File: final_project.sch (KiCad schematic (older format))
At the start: 0 parts

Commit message: Merged 8254
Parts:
- added C1: 100uF, symbol pspice:C
- added J1: Conn_01x02_Female, symbol Connector:Conn_01x02_Female
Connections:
- new net +5V: C1.1, J1.1 (Pin_1)
- new net GND: C1.2, J1.2 (Pin_2)

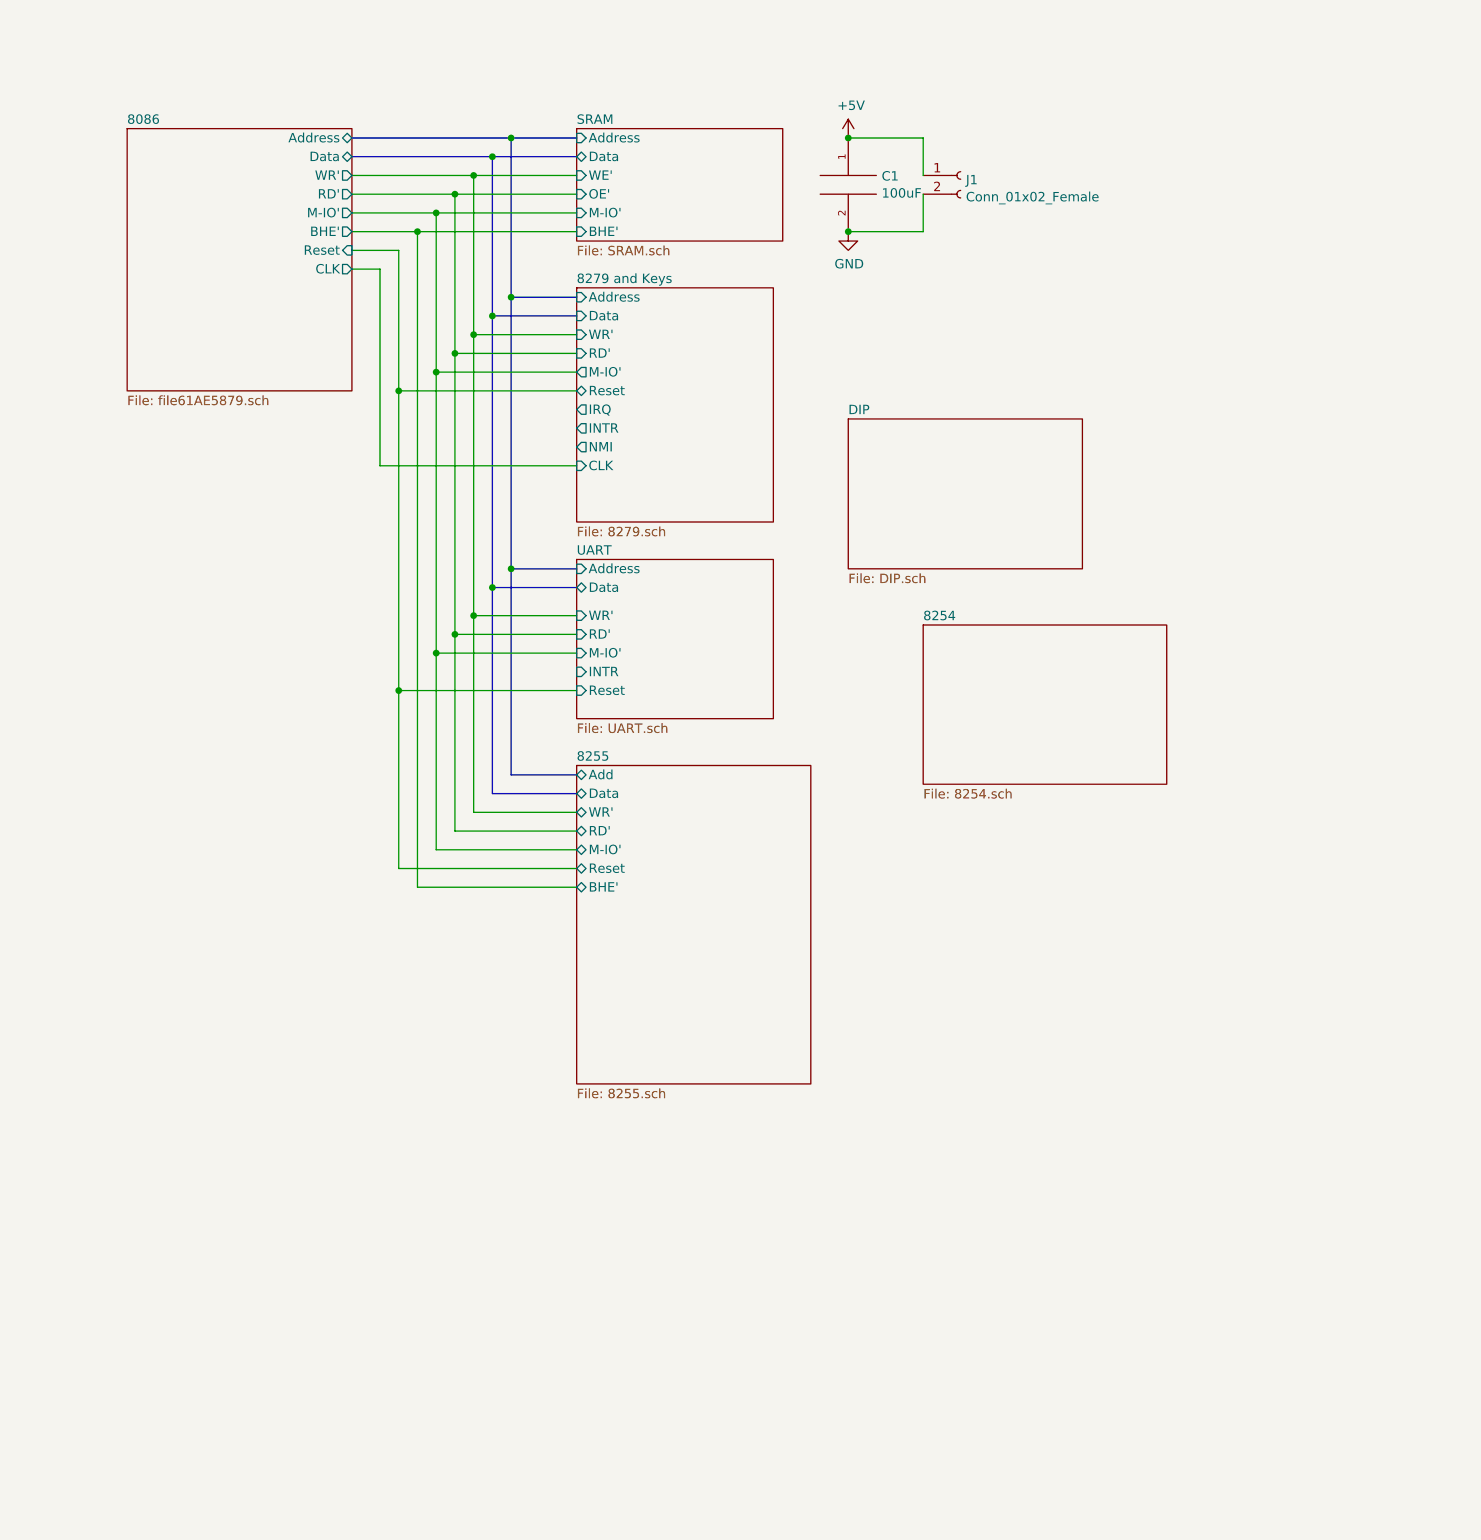
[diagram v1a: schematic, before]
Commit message: Integrated LCD.  Fixed issues with busses
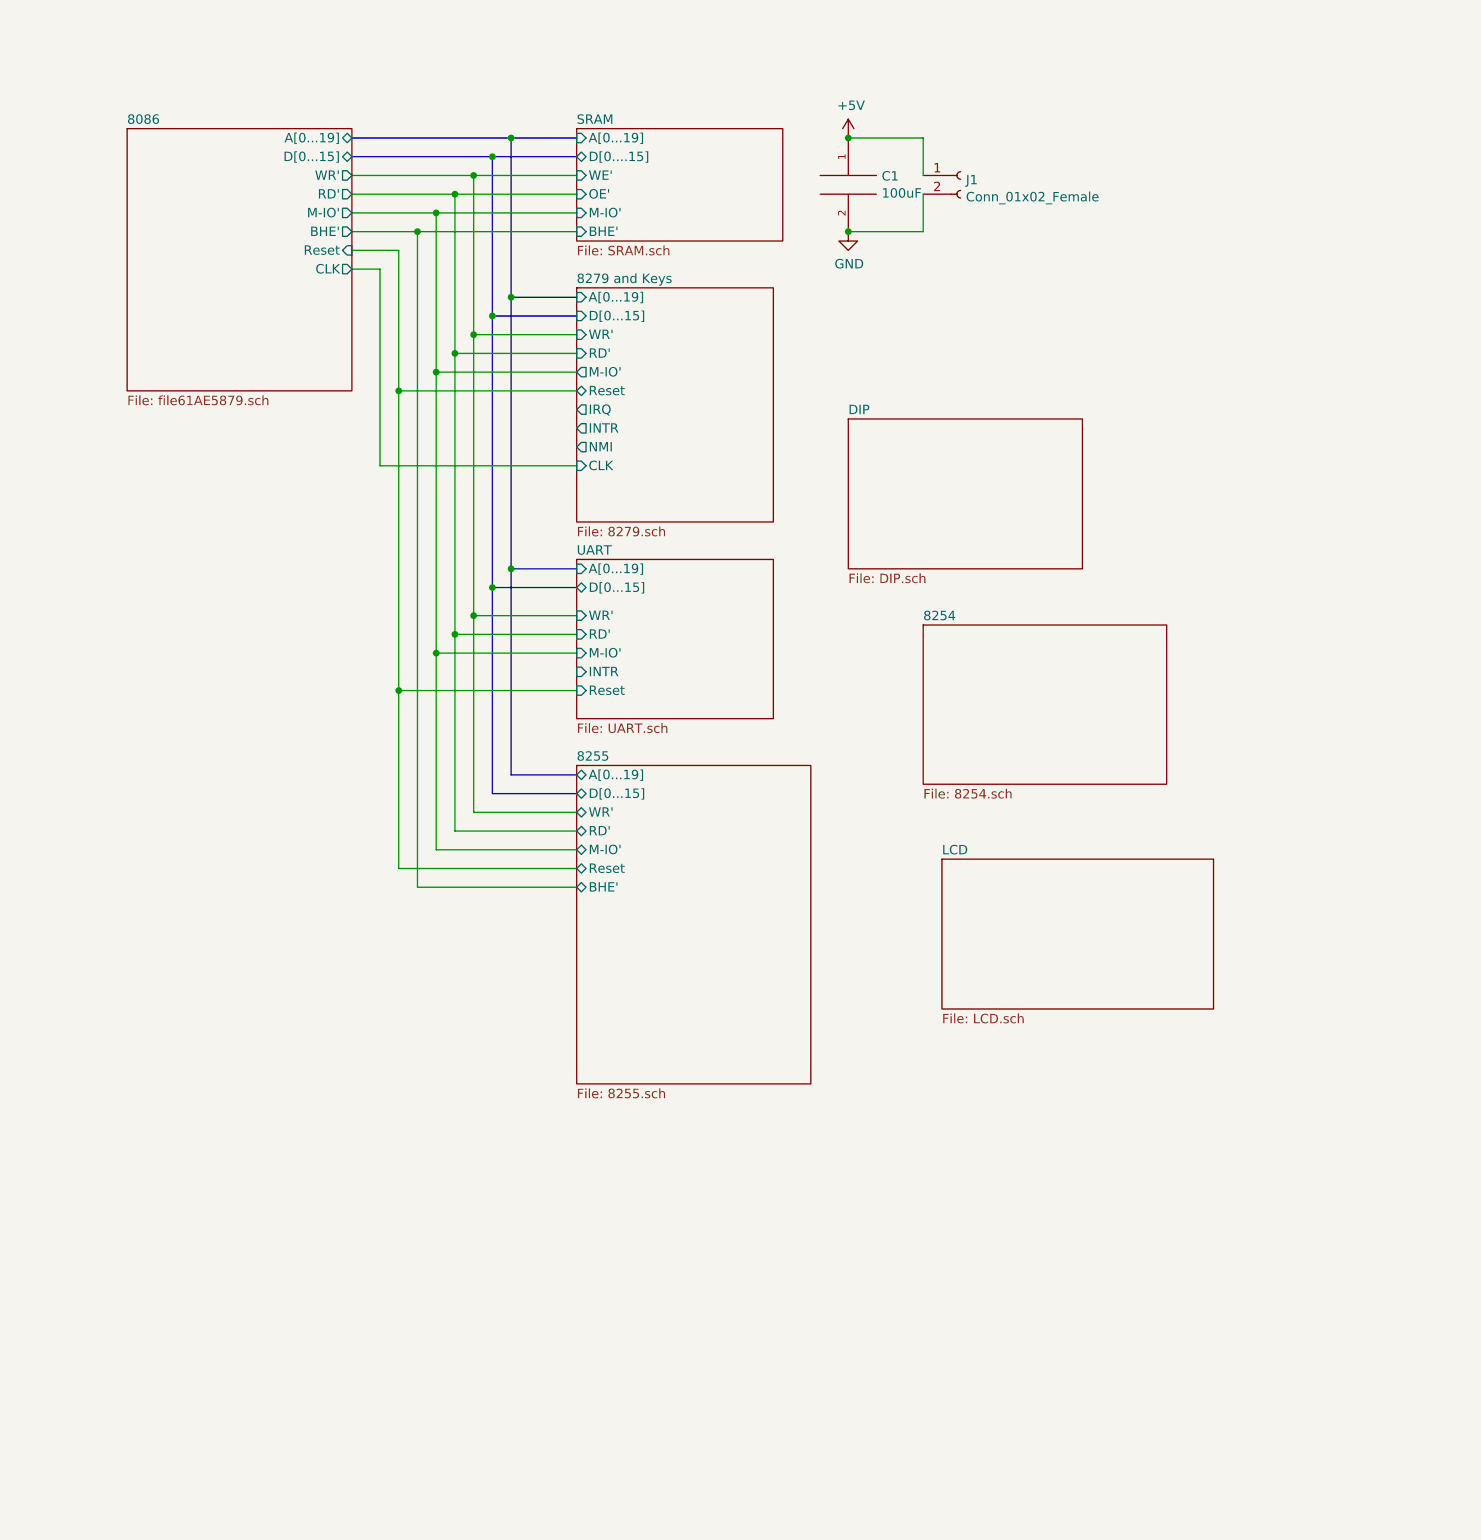
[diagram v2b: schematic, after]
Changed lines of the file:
@@
 $Descr A4 11693 8268
 encoding utf-8
-Sheet 1 8
+Sheet 1 9
 Title ""
 Date ""
@@
 F0 "8086" 50
 F1 "file61AE5879.sch" 50
-F2 "Data" B R 2400 1300 50
-F3 "Address" B R 2400 1200 50
+F2 "D[0...15]" B R 2400 1300 50
+F3 "A[0...19]" B R 2400 1200 50
 F4 "M-IO'" O R 2400 1600 50
 F5 "WR'" O R 2400 1400 50
@@
 F0 "8255" 50
 F1 "8255.sch" 50
-F2 "Data" B L 3600 4700 50
-F3 "Add" B L 3600 4600 50
+F2 "D[0...15]" B L 3600 4700 50
+F3 "A[0...19]" B L 3600 4600 50
 F4 "WR'" B L 3600 4800 50
 F5 "RD'" B L 3600 4900 50
@@
 F0 "8279 and Keys" 50
 F1 "8279.sch" 50
-F2 "Address" I L 3600 2050 50
-F3 "Data" I L 3600 2150 50
+F2 "A[0...19]" I L 3600 2050 50
+F3 "D[0...15]" I L 3600 2150 50
 F4 "WR'" I L 3600 2250 50
 F5 "RD'" I L 3600 2350 50
@@
 F0 "UART" 50
 F1 "UART.sch" 50
-F2 "Data" B L 3600 3600 50
-F3 "Address" I L 3600 3500 50
+F2 "D[0...15]" B L 3600 3600 50
+F3 "A[0...19]" I L 3600 3500 50
 F4 "WR'" I L 3600 3750 50
 F5 "RD'" I L 3600 3850 50
@@
 F2 "BHE'" I L 3600 1700 50
 F3 "WE'" I L 3600 1400 50
-F4 "Address" I L 3600 1200 50
+F4 "A[0...19]" I L 3600 1200 50
 F5 "M-IO'" I L 3600 1600 50
-F6 "Data" B L 3600 1300 50
+F6 "D[0....15]" B L 3600 1300 50
 F7 "OE'" I L 3600 1500 50
 $EndSheet
@@
 $EndComp
 $Comp
-L power:GND #PWR0101
+L power:GND #PWR02
 U 1 1 625BB158
 P 5050 1700
-F 0 "#PWR0101" H 5050 1450 50  0001 C CNN
+F 0 "#PWR02" H 5050 1450 50  0001 C CNN
 F 1 "GND" H 5055 1527 50  0000 C CNN
 F 2 "" H 5050 1700 50  0001 C CNN
@@
 $EndComp
 $Comp
-L power:+5V #PWR0102
+L power:+5V #PWR01
 U 1 1 625BB5A4
 P 5050 1200
-F 0 "#PWR0102" H 5050 1050 50  0001 C CNN
+F 0 "#PWR01" H 5050 1050 50  0001 C CNN
 F 1 "+5V" H 5065 1373 50  0000 C CNN
 F 2 "" H 5050 1200 50  0001 C CNN
@@
 F1 "8254.sch" 50
 $EndSheet
+$Sheet
+S 5550 5050 1450 800
+U 61E46856
+F0 "LCD" 50
+F1 "LCD.sch" 50
+$EndSheet
 $EndSCHEMATC

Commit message: All schematics present
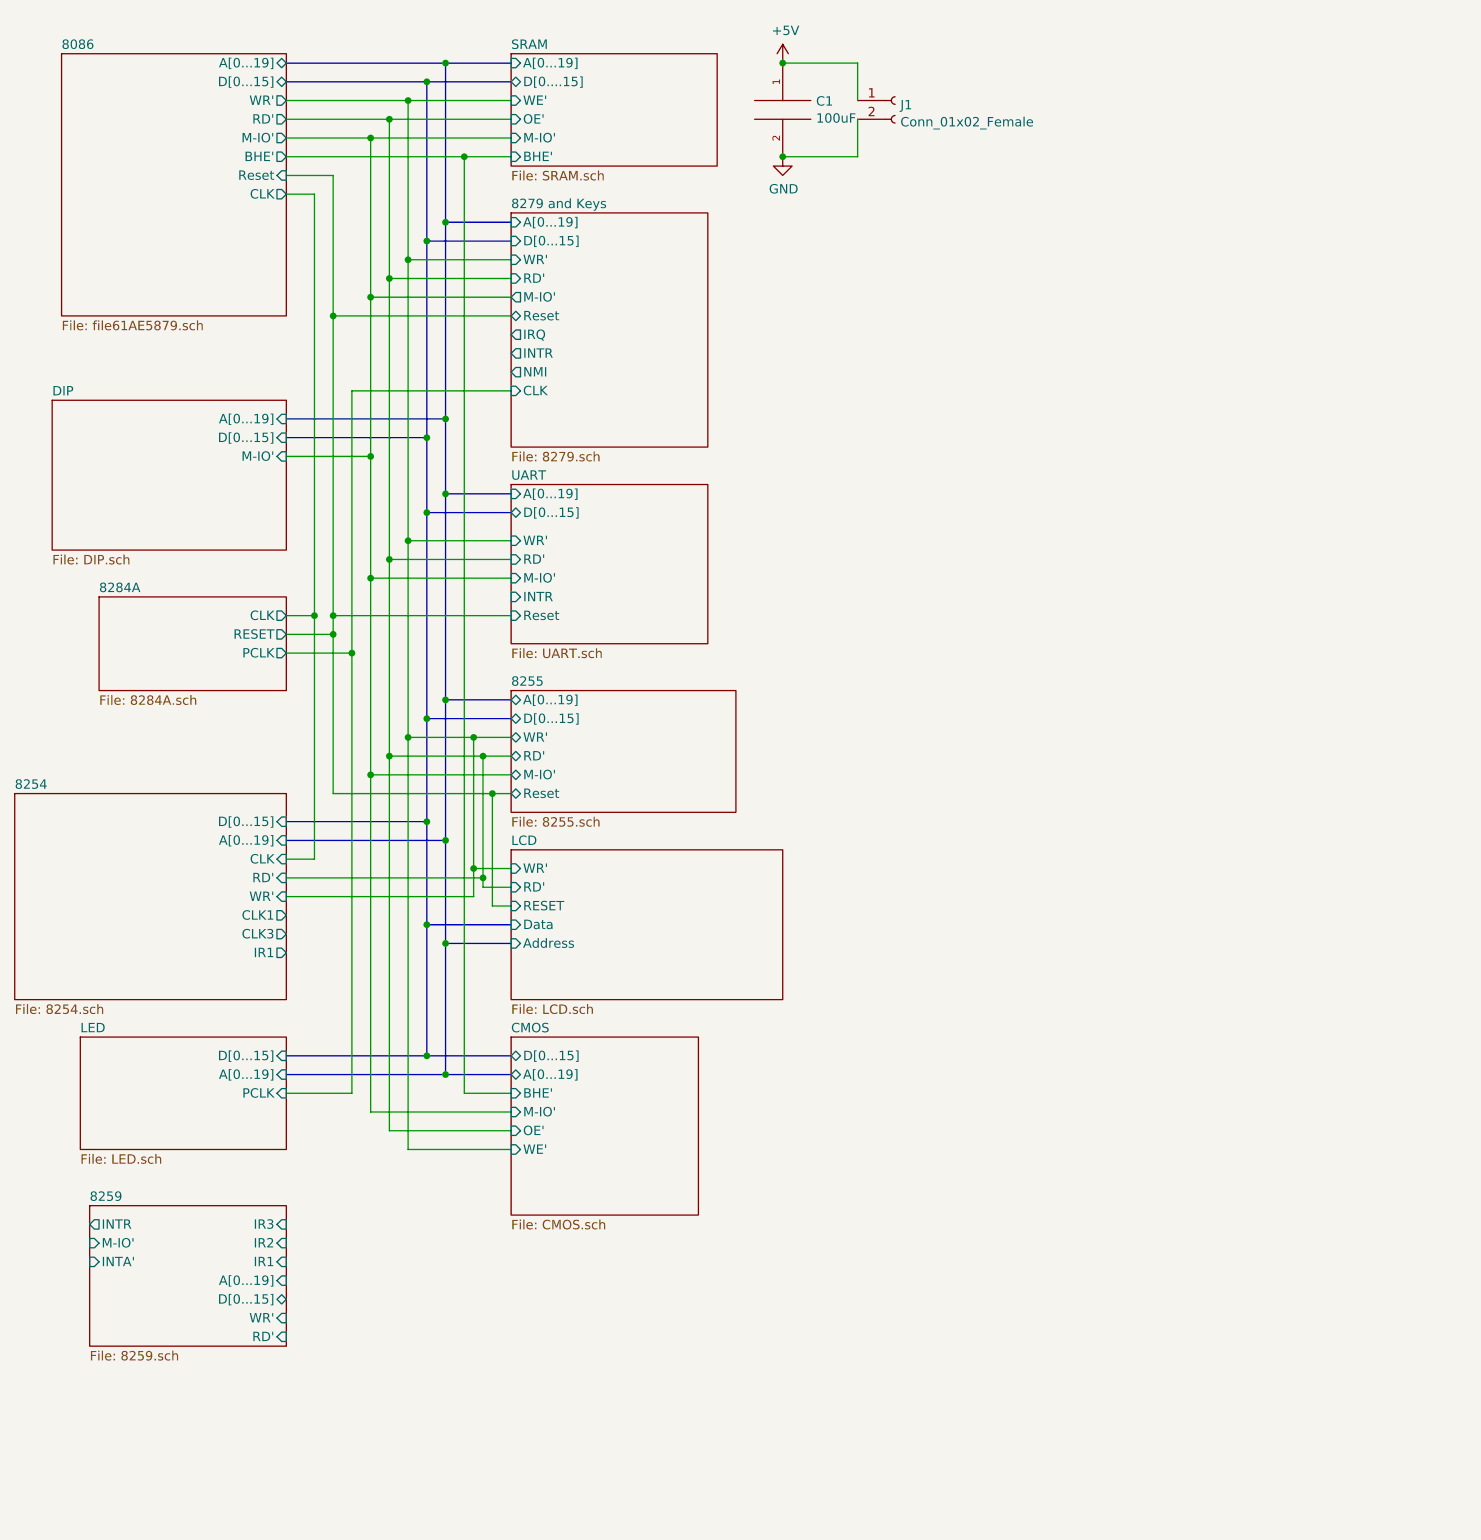
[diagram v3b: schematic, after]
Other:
- moved on the sheet: C1, J1

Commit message: Wired Root
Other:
- moved on the sheet: C1, J1

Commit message: Started PCB
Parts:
- added R1: R, Resistor_SMD:R_0201_0603Metric, symbol Device:R
- C1: footprint (none) -> Capacitor_SMD:CP_Elec_3x5.3
- J1: footprint (none) -> Connector:Banana_Jack_1Pin
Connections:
- net +5V: now also R1.1
- new net +3V3: R1.2
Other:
- moved on the sheet: C1, J1
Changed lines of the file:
@@
 L Connector:Conn_01x02_Female J1
 U 1 1 625BA044
-P 6450 1100
-F 0 "J1" H 6478 1076 50  0000 L CNN
-F 1 "Conn_01x02_Female" H 6478 985 50  0000 L CNN
-F 2 "" H 6450 1100 50  0001 C CNN
-F 3 "~" H 6450 1100 50  0001 C CNN
-	1    6450 1100
+P 6850 1150
+F 0 "J1" H 6878 1126 50  0000 L CNN
+F 1 "Conn_01x02_Female" H 6878 1035 50  0000 L CNN
+F 2 "Connector:Banana_Jack_1Pin" H 6850 1150 50  0001 C CNN
+F 3 "~" H 6850 1150 50  0001 C CNN
+	1    6850 1150
 	1    0    0    -1
 $EndComp
 $Comp
-L power:GND #PWR02
+L power:GND #PWR03
 U 1 1 625BB158
-P 5850 1400
-F 0 "#PWR02" H 5850 1150 50  0001 C CNN
-F 1 "GND" H 5855 1227 50  0000 C CNN
-F 2 "" H 5850 1400 50  0001 C CNN
-F 3 "" H 5850 1400 50  0001 C CNN
-	1    5850 1400
+P 6250 1450
+F 0 "#PWR03" H 6250 1200 50  0001 C CNN
+F 1 "GND" H 6255 1277 50  0000 C CNN
+F 2 "" H 6250 1450 50  0001 C CNN
+F 3 "" H 6250 1450 50  0001 C CNN
+	1    6250 1450
 	1    0    0    -1
 $EndComp
 $Comp
-L power:+5V #PWR01
+L power:+5V #PWR02
 U 1 1 625BB5A4
-P 5850 900
-F 0 "#PWR01" H 5850 750 50  0001 C CNN
-F 1 "+5V" H 5865 1073 50  0000 C CNN
-F 2 "" H 5850 900 50  0001 C CNN
-F 3 "" H 5850 900 50  0001 C CNN
-	1    5850 900
+P 6250 950
+F 0 "#PWR02" H 6250 800 50  0001 C CNN
+F 1 "+5V" H 6265 1123 50  0000 C CNN
+F 2 "" H 6250 950 50  0001 C CNN
+F 3 "" H 6250 950 50  0001 C CNN
+	1    6250 950
 	1    0    0    -1
 $EndComp
@@
 L pspice:C C1
 U 1 1 625BBC2C
-P 5850 1150
-F 0 "C1" H 6028 1196 50  0000 L CNN
-F 1 "100uF" H 6028 1105 50  0000 L CNN
-F 2 "" H 5850 1150 50  0001 C CNN
-F 3 "~" H 5850 1150 50  0001 C CNN
-	1    5850 1150
+P 6250 1200
+F 0 "C1" H 6428 1246 50  0000 L CNN
+F 1 "100uF" H 6428 1155 50  0000 L CNN
+F 2 "Capacitor_SMD:CP_Elec_3x5.3" H 6250 1200 50  0001 C CNN
+F 3 "~" H 6250 1200 50  0001 C CNN
+	1    6250 1200
 	1    0    0    -1
 $EndComp
 Wire Wire Line
-	5850 1400 6250 1400
-Wire Wire Line
-	6250 1400 6250 1200
-Connection ~ 5850 1400
-Connection ~ 5850 900
-Wire Wire Line
-	6250 900  5850 900
-Wire Wire Line
-	6250 1100 6250 900
+	6250 1450 6650 1450
+Wire Wire Line
+	6650 1450 6650 1250
+Connection ~ 6250 1450
+Connection ~ 6250 950
+Wire Wire Line
+	6650 950  6250 950
+Wire Wire Line
+	6650 1150 6650 950
 $Sheet
 S 1950 2700 1250 800
@@
 F3 "RD'" I L 4400 5300 50
 F4 "RESET" I L 4400 5400 50
-F5 "Data" I L 4400 5500 50
-F6 "Address" I L 4400 5600 50
+F5 "D[0...15]" I L 4400 5500 50
+F6 "A[0...19]" I L 4400 5600 50
 $EndSheet
 $Sheet
@@
 Wire Wire Line
 	1700 1800 2000 1800
+$Comp
+L Device:R R1
+U 1 1 630D38E8
+P 6100 950
+F 0 "R1" V 5893 950 50  0000 C CNN
+F 1 "R" V 5984 950 50  0000 C CNN
+F 2 "Resistor_SMD:R_0201_0603Metric" V 6030 950 50  0001 C CNN
+F 3 "~" H 6100 950 50  0001 C CNN
+	1    6100 950
+	0    1    1    0
+$EndComp
+$Comp
+L power:+3.3V #PWR01
+U 1 1 630D8F6E
+P 5950 950
+F 0 "#PWR01" H 5950 800 50  0001 C CNN
+F 1 "+3.3V" V 5965 1078 50  0000 L CNN
+F 2 "" H 5950 950 50  0001 C CNN
+F 3 "" H 5950 950 50  0001 C CNN
+	1    5950 950
+	0    -1   -1   0
+$EndComp
 $EndSCHEMATC

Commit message: Readd LCD changes.
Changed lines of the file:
@@
 Connection ~ 3450 2250
-Wire Wire Line
-	4400 4800 4300 4800
 Wire Wire Line
 	3450 4800 3450 3950
@@
 F0 "LCD" 50
 F1 "LCD.sch" 50
-F2 "WR'" I L 4400 5200 50
-F3 "RD'" I L 4400 5300 50
-F4 "RESET" I L 4400 5400 50
-F5 "D[0...15]" I L 4400 5500 50
-F6 "A[0...19]" I L 4400 5600 50
+F2 "D[0...15]" I L 4400 5200 50
+F3 "A[0...19]" I L 4400 5300 50
 $EndSheet
 $Sheet
@@
 	3950 4400 3950 4950
 Wire Bus Line
-	3950 5500 4400 5500
+	3950 5200 4400 5200
 Connection ~ 3950 4400
 Wire Bus Line
-	4400 5600 4050 5600
-Wire Bus Line
-	4050 5600 4050 5050
+	4400 5300 4050 5300
 Connection ~ 4050 4300
-Wire Wire Line
-	4400 5400 4300 5400
-Wire Wire Line
-	4300 5400 4300 4800
-Connection ~ 4300 4800
-Wire Wire Line
-	4300 4800 3450 4800
-Wire Wire Line
-	4400 5300 4250 5300
-Wire Wire Line
-	4250 5300 4250 5250
 Connection ~ 4250 4600
-Wire Wire Line
-	4400 5200 4200 5200
-Wire Wire Line
-	4200 5200 4200 4500
 Connection ~ 4200 4500
 Wire Wire Line
 	4200 4500 4400 4500
 Wire Bus Line
-	3950 5500 3950 6200
-Wire Bus Line
 	3950 6200 4400 6200
-Connection ~ 3950 5500
 Wire Bus Line
 	4400 6300 4050 6300
-Wire Bus Line
-	4050 6300 4050 5600
-Connection ~ 4050 5600
 Wire Wire Line
 	3650 4700 3650 6500
@@
 Connection ~ 3950 4950
 Wire Bus Line
-	3950 4950 3950 5500
-Wire Bus Line
 	3200 5050 4050 5050
 Connection ~ 4050 5050
@@
 Connection ~ 3350 3850
 Wire Wire Line
-	3200 5250 4250 5250
-Connection ~ 4250 5250
-Wire Wire Line
 	4250 5250 4250 4600
 Wire Wire Line
 	3200 5350 4200 5350
-Wire Wire Line
-	4200 5350 4200 5200
-Connection ~ 4200 5200
 $Sheet
 S 2100 6100 1100 600
@@
 	0    -1   -1   0
 $EndComp
+Wire Wire Line
+	4200 4500 4200 5350
+Wire Wire Line
+	3450 4800 4400 4800
+Connection ~ 3950 5200
+Wire Bus Line
+	3950 5200 3950 6200
+Connection ~ 4050 5300
+Wire Bus Line
+	4050 5300 4050 6300
+Wire Bus Line
+	3950 4950 3950 5200
+Wire Wire Line
+	3200 5250 4250 5250
+Wire Bus Line
+	4050 5050 4050 5300
 $EndSCHEMATC

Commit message: Bleh
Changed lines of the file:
@@
 L power:+5V #PWR02
 U 1 1 625BB5A4
-P 6250 950
-F 0 "#PWR02" H 6250 800 50  0001 C CNN
-F 1 "+5V" H 6265 1123 50  0000 C CNN
-F 2 "" H 6250 950 50  0001 C CNN
-F 3 "" H 6250 950 50  0001 C CNN
-	1    6250 950
+P 6650 950
+F 0 "#PWR02" H 6650 800 50  0001 C CNN
+F 1 "+5V" H 6665 1123 50  0000 C CNN
+F 2 "" H 6650 950 50  0001 C CNN
+F 3 "" H 6650 950 50  0001 C CNN
+	1    6650 950
 	1    0    0    -1
 $EndComp
@@
 L power:+3.3V #PWR01
 U 1 1 630D8F6E
-P 5950 950
-F 0 "#PWR01" H 5950 800 50  0001 C CNN
-F 1 "+3.3V" V 5965 1078 50  0000 L CNN
-F 2 "" H 5950 950 50  0001 C CNN
-F 3 "" H 5950 950 50  0001 C CNN
-	1    5950 950
-	0    -1   -1   0
+P 5900 950
+F 0 "#PWR01" H 5900 800 50  0001 C CNN
+F 1 "+3.3V" V 5915 1078 50  0000 L CNN
+F 2 "" H 5900 950 50  0001 C CNN
+F 3 "" H 5900 950 50  0001 C CNN
+	1    5900 950
+	1    0    0    -1
 $EndComp
 Wire Wire Line
@@
 Wire Bus Line
 	4050 5050 4050 5300
+Connection ~ 6650 950
+Wire Wire Line
+	5950 950  5900 950
 $EndSCHEMATC
